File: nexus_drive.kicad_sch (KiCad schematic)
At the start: 0 parts

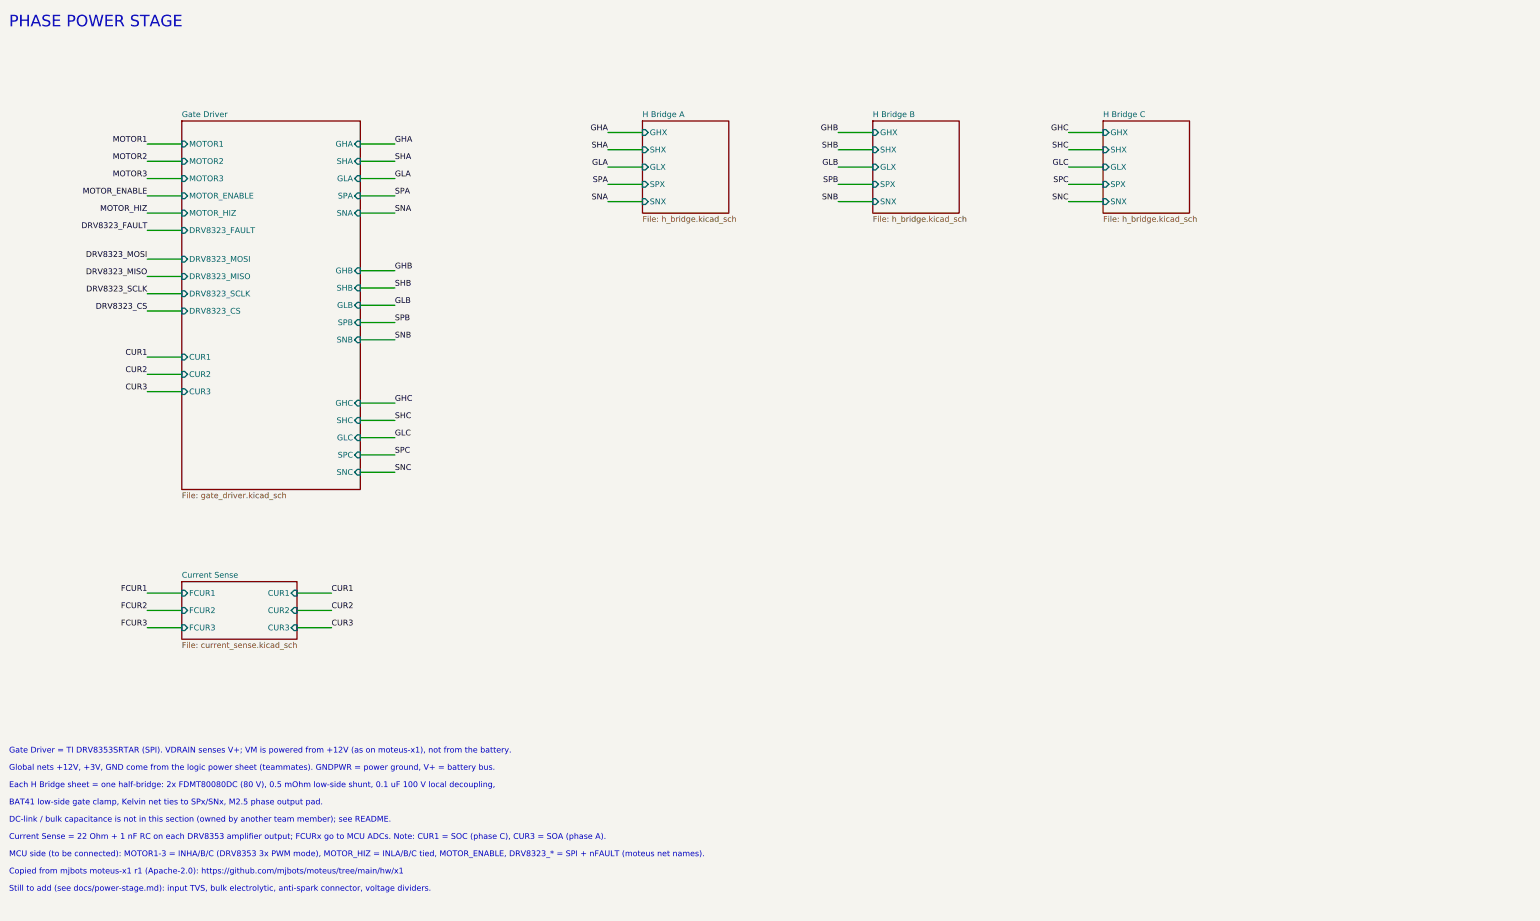
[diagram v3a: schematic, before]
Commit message: Add STM32G474METx MCU sheet wired to the pin plan
MCU sheet follows Comms Component Selection.ioc. Gate driver switched to
6-PWM (INLA/B/C split from MOTOR_HIZ) to match TIM1 CHx/CHxN. Root nets
renamed to the pin-plan names (PWM_xH/xL, GATE_EN, DRV_*, CURR_A/B/C).

Co-Authored-By: Claude Opus 5.5 <noreply@anthropic.com>
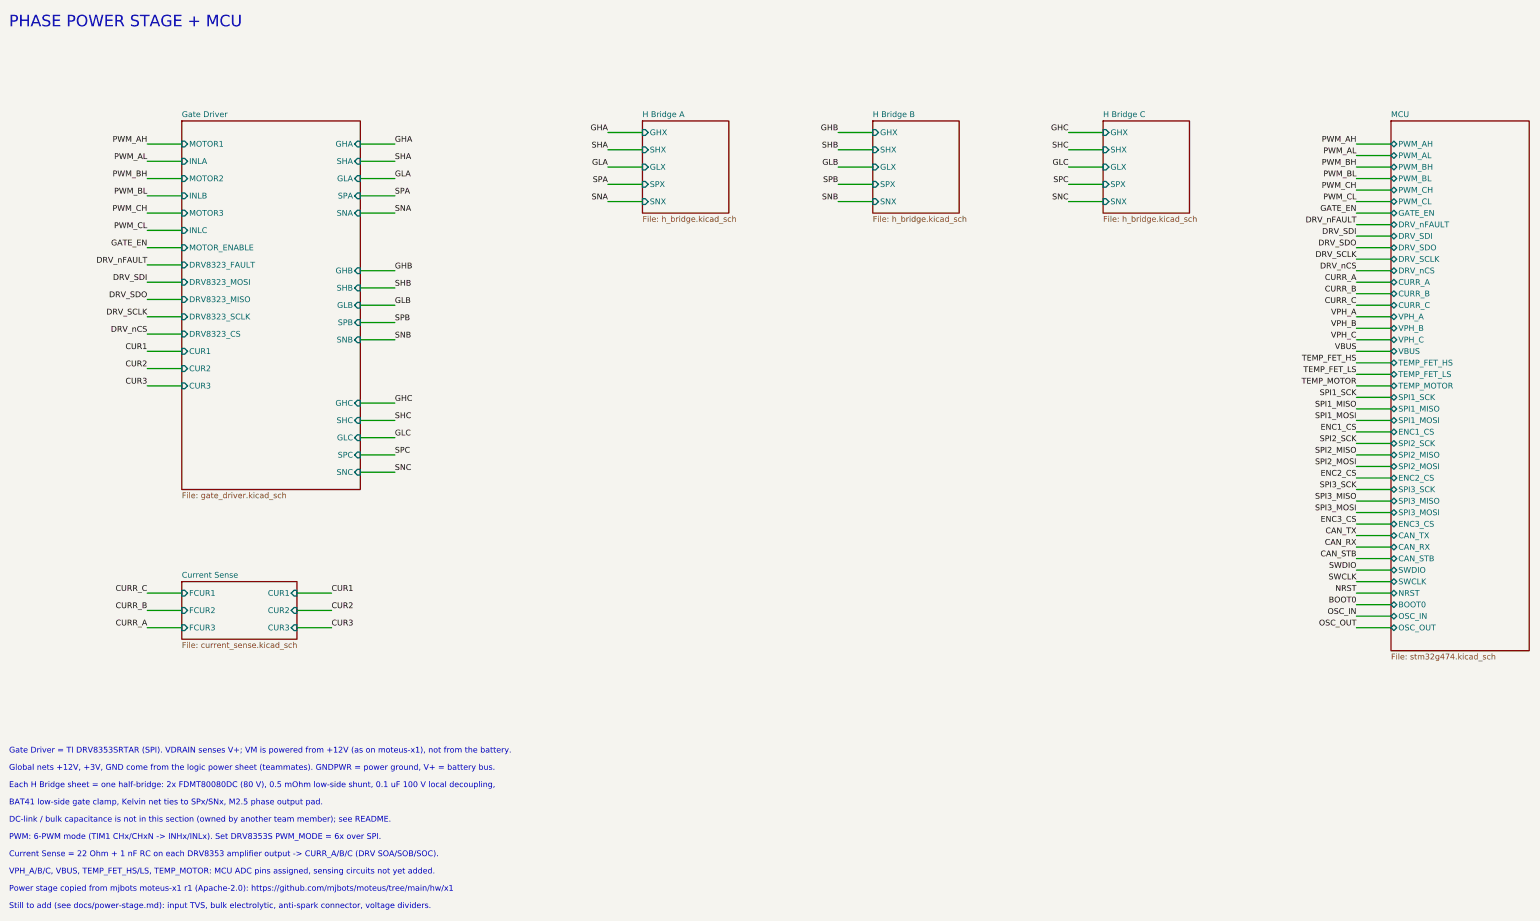
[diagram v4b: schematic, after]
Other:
- added sheet MCU (stm32g474.kicad_sch)
- sheet Gate Driver ports: added INLA, INLB, INLC; removed MOTOR_HIZ
- note added: "Current Sense = 22 Ohm + 1 nF RC on each DRV8353 amplifier output -> CURR_A/B/C (DRV SOA/SOB/SOC)."
- note added: "PHASE POWER STAGE + MCU"
- note added: "PWM: 6-PWM mode (TIM1 CHx/CHxN -> INHx/INLx). Set DRV8353S PWM_MODE = 6x over SPI."
- note added: "Power stage copied from mjbots moteus-x1 r1 (Apache-2.0): https://github.com/mjbots/moteus/tree/main/hw/x1"
- note added: "VPH_A/B/C, VBUS, TEMP_FET_HS/LS, TEMP_MOTOR: MCU ADC pins assigned, sensing circuits not yet added."
- note removed: "Copied from mjbots moteus-x1 r1 (Apache-2.0): https://github.com/mjbots/moteus/tree/main/hw/x1"
- note removed: "Current Sense = 22 Ohm + 1 nF RC on each DRV8353 amplifier output; FCURx go to MCU ADCs. Note: CUR1 = SOC (phase C), CUR3 = SOA (phase A)."
- note removed: "MCU side (to be connected): MOTOR1-3 = INHA/B/C (DRV8353 3x PWM mode), MOTOR_HIZ = INLA/B/C tied, MOTOR_ENABLE, DRV8323_* = SPI + nFAULT (moteus net names)."
- note removed: "PHASE POWER STAGE"

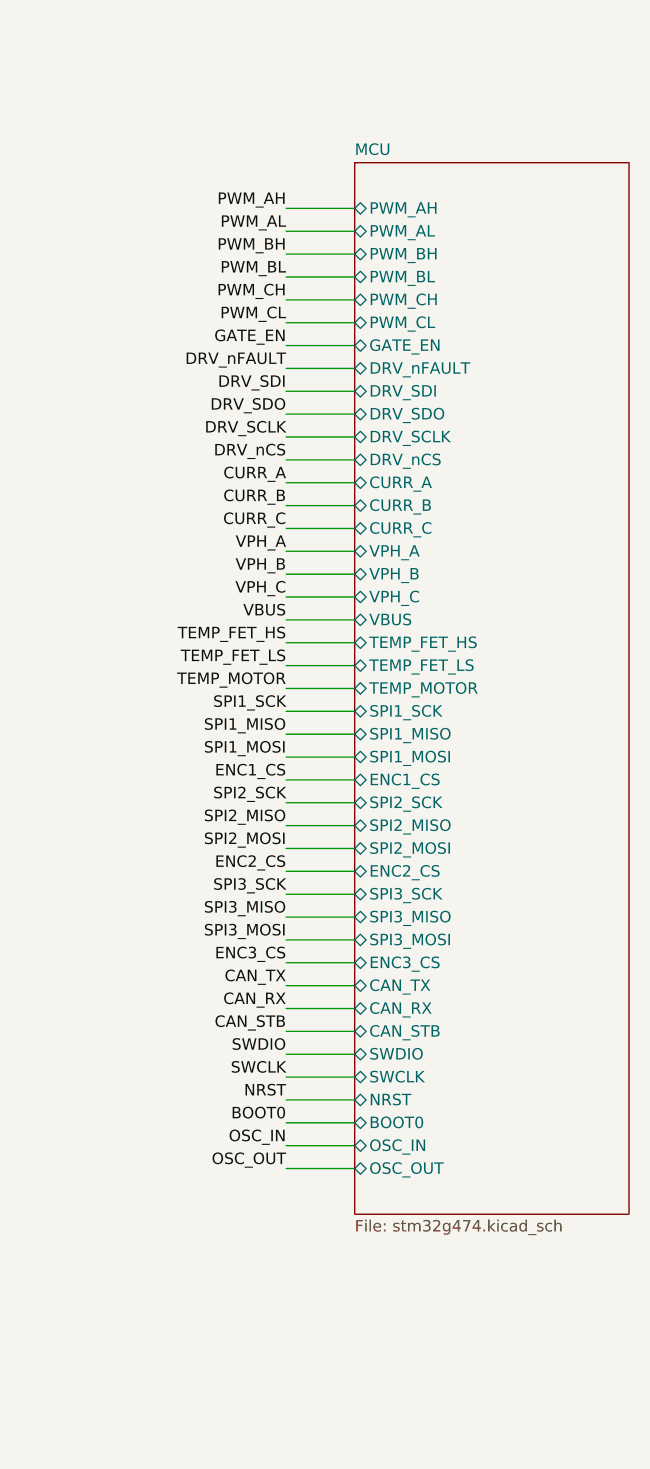
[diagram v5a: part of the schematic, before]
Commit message: Fix MCU power wiring and add USART3 sheet pins
Reconnect the +3V rail (shifted off the VBAT/VDDA stubs), add the missing
VREF+ and VSS wires, and add USART3_TX/RX pins to the MCU sheet symbol.

Co-Authored-By: Claude Opus 5.5 <noreply@anthropic.com>
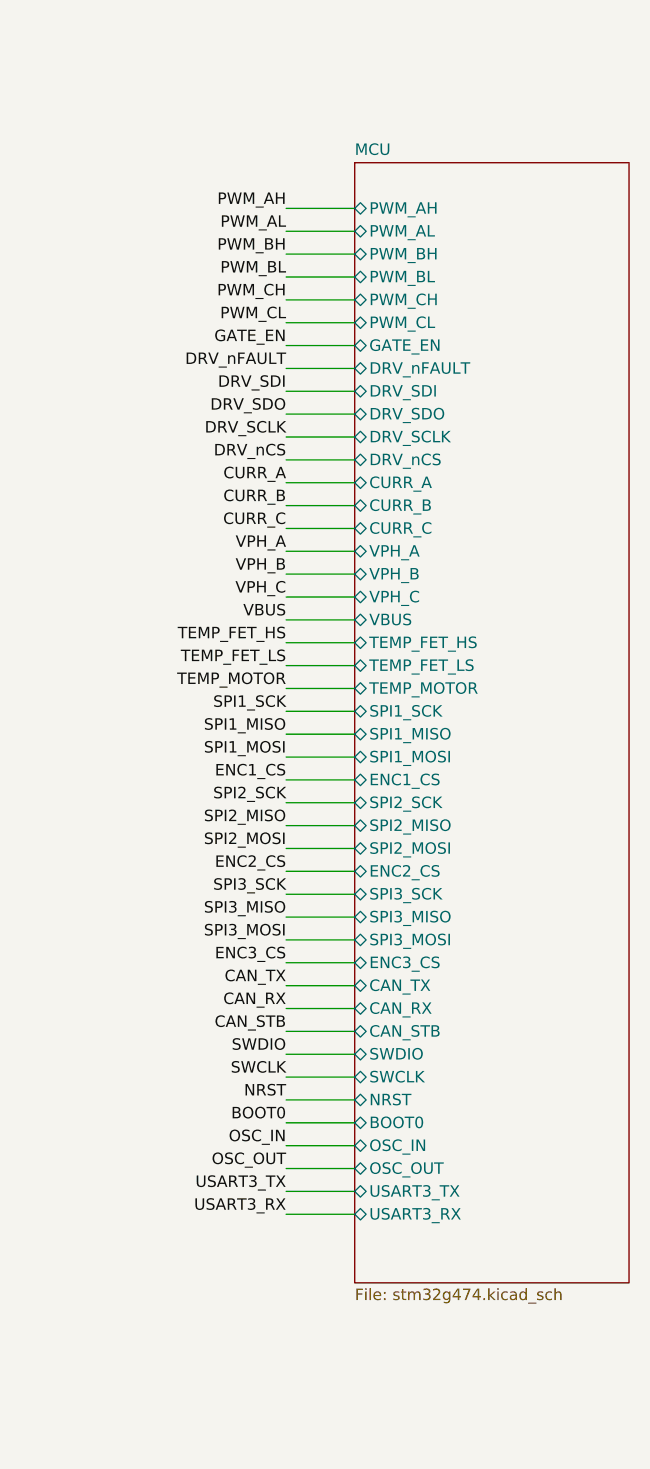
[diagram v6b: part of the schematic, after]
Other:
- sheet MCU ports: added USART3_RX, USART3_TX; removed none
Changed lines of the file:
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@@
+		)
+	)
+	(wire
+		(pts
+			(xy 322.58 165.1) (xy 330.2 165.1)
+		)
+		(stroke
+			(width 0)
+			(type default)
+		)
+	)
+	(label "USART3_TX"
+		(at 322.58 165.1 180)
+		(effects
+			(font
+				(size 1.27 1.27)
+			)
+			(justify right bottom)
+		)
+	)
+	(wire
+		(pts
+			(xy 322.58 167.64) (xy 330.2 167.64)
+		)
+		(stroke
+			(width 0)
+			(type default)
+		)
+	)
+	(label "USART3_RX"
+		(at 322.58 167.64 180)
+		(effects
+			(font
+				(size 1.27 1.27)
+			)
+			(justify right bottom)
 		)
 	)
@@
 	(sheet
 		(at 330.2 50.8)
-		(size 30.48 116.84)
+		(size 30.48 124.46)
 		(exclude_from_sim no)
 		(in_bom yes)
@@
 		)
 		(property "Sheetfile" "stm32g474.kicad_sch"
-			(at 330.2 168.2246 0)
+			(at 330.2 175.8446 0)
 			(show_name no)
 			(do_not_autoplace no)
@@
 			(effects
 				(font
+					(size 1.27 1.27)
+				)
+				(justify left)
+			)
+		)
+		(pin "USART3_TX" bidirectional
+			(at 330.2 165.1 180)
+			(effects
+				(font
+					(size 1.27 1.27)
+				)
+				(justify left)
+			)
+		)
+		(pin "USART3_RX" bidirectional
+			(at 330.2 167.64 180)
+			(effects
+				(font
